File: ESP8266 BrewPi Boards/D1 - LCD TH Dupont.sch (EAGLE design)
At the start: 7 parts, among them J1 RJ45-8X

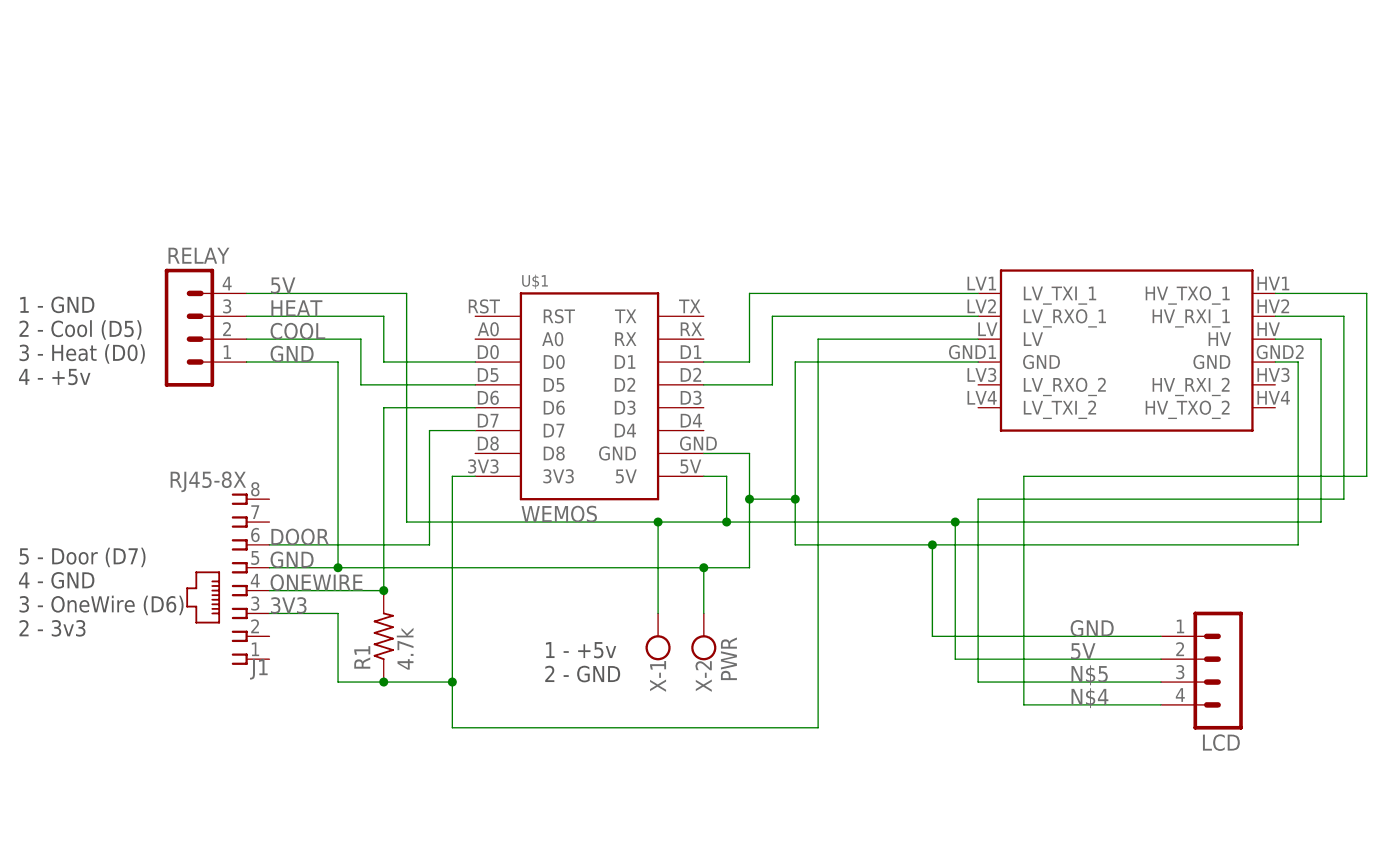
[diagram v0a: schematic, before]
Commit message: Updating LCD TH Dupont design
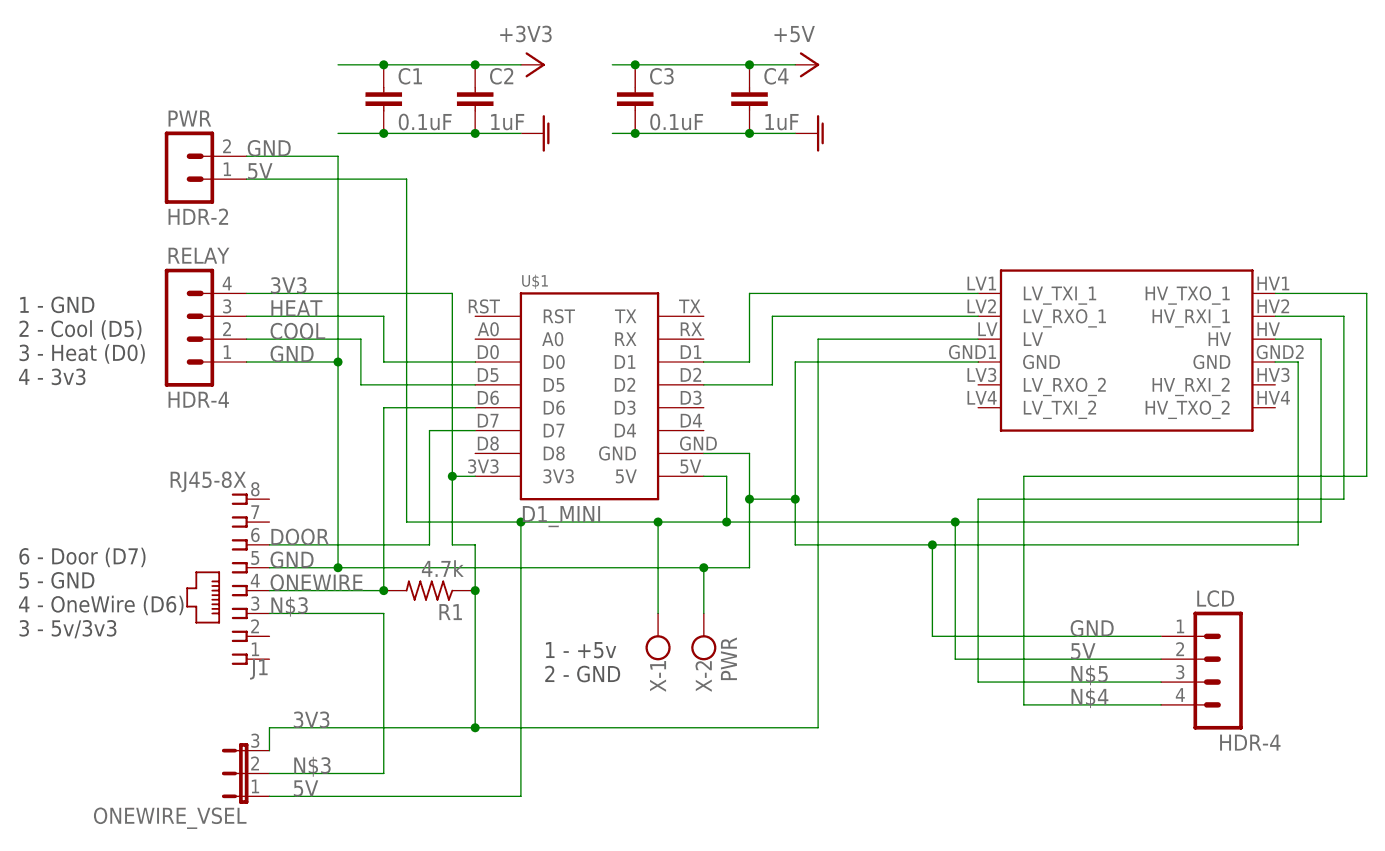
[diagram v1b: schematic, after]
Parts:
- added C1, C3: 0.1uF, rcl:C-EU050-035X075
- added C2, C4: 1uF, rcl:C-EU050-035X075
- added ONEWIRE_VSEL: (no value), Donnie:JP2ENOLABEL
- added PWR: HDR-2, Donnie:HDR-2
- LCD, RELAY: value (none) -> HDR-4; device con-lstb:MA04-1 -> Donnie:HDR-4
- U$1: value WEMOS -> D1_MINI; device 1455413453956-wemos:WEMOS -> 1455413453956-wemos:WEMOSCLEAN
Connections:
- new net N$3: J1.3, ONEWIRE_VSEL.2
- net 3V3: now also C1.1, C2.1, ONEWIRE_VSEL.3, RELAY.4; no longer J1.3
- net 5V: now also C3.1, C4.1, ONEWIRE_VSEL.1, PWR.1; no longer RELAY.4
- net GND: now also C1.2, C2.2, C3.2, C4.2, PWR.2
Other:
- note added: "1 - GND 2 - Cool (D5) 3 - Heat (D0) 4 - 3v3"
- note added: "6 - Door (D7) 5 - GND 4 - OneWire (D6) 3 - 5v/3v3"
- note removed: "1 - GND 2 - Cool (D5) 3 - Heat (D0) 4 - +5v"
- note removed: "5 - Door (D7) 4 - GND 3 - OneWire (D6) 2 - 3v3"
- moved on the sheet: R1

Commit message: Updating board designs and adding DirtyPCB Links
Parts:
- J1: device con-tycoelectronics:RJ45-8X -> Donnie:RJ45-8X
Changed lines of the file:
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@@
 <part name="U$1" library="1455413453956-wemos" deviceset="WEMOS" device="CLEAN" value="D1_MINI"/>
 <part name="X" library="con-wago-500" deviceset="W237-102" device="" value="PWR"/>
-<part name="J1" library="con-tycoelectronics" library_urn="urn:adsk.eagle:library:193" deviceset="RJ45" device="" package3d_urn="urn:adsk.eagle:package:10660/1" technology="-8X"/>
+<part name="J1" library="Donnie" deviceset="RJ45" device="" package3d_urn="urn:adsk.eagle:package:10660/1" technology="-8X"/>
 <part name="R1" library="rcl" library_urn="urn:adsk.eagle:library:334" deviceset="R-US_" device="0309/12" package3d_urn="urn:adsk.eagle:package:23571/1" value="4.7k"/>
 <part name="U$3" library="SparkFun-Boards" library_urn="urn:adsk.eagle:library:509" deviceset="SPARKFUN_LOGIC_LEVEL_CONVERTER" device="" package3d_urn="urn:adsk.eagle:package:37318/1"/>
